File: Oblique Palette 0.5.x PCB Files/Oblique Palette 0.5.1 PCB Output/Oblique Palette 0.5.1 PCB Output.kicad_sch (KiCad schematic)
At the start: 16 parts, among them J40 Conn_01x03_Female_Pin, J42 AudioJack2_SwitchT, U11 MCP4725xxx-xCH, U12 MCP6004

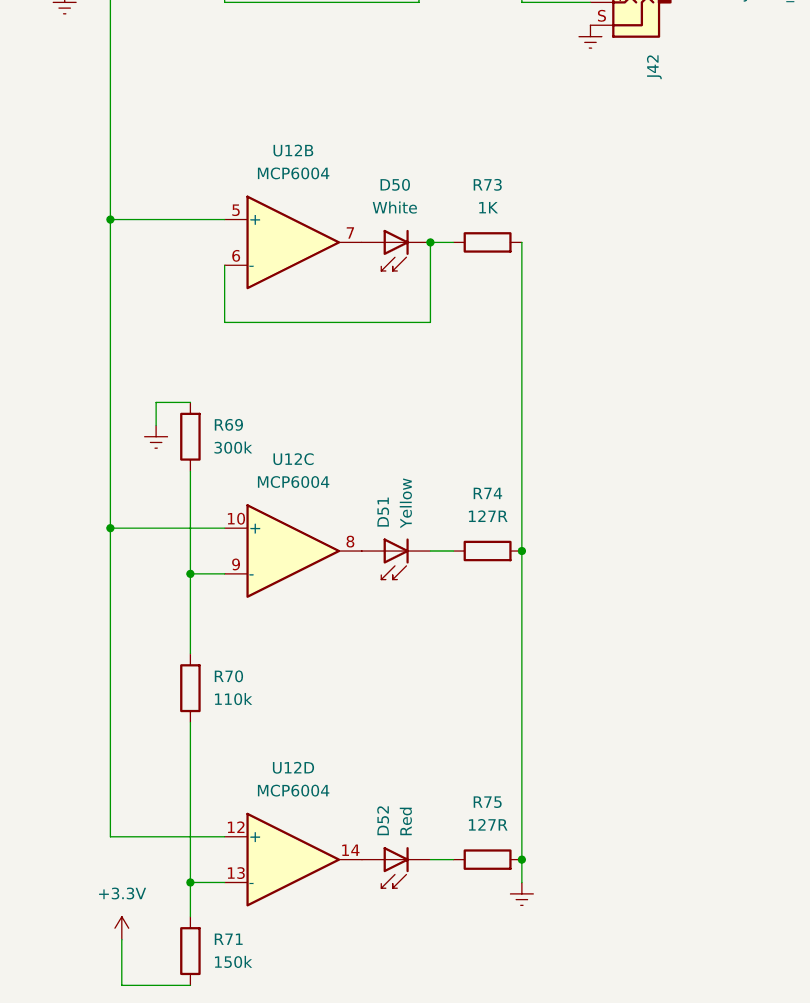
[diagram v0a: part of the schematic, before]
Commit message: Ready to go, but for some blank part numbers in the BOM to work out with the manufacturer.
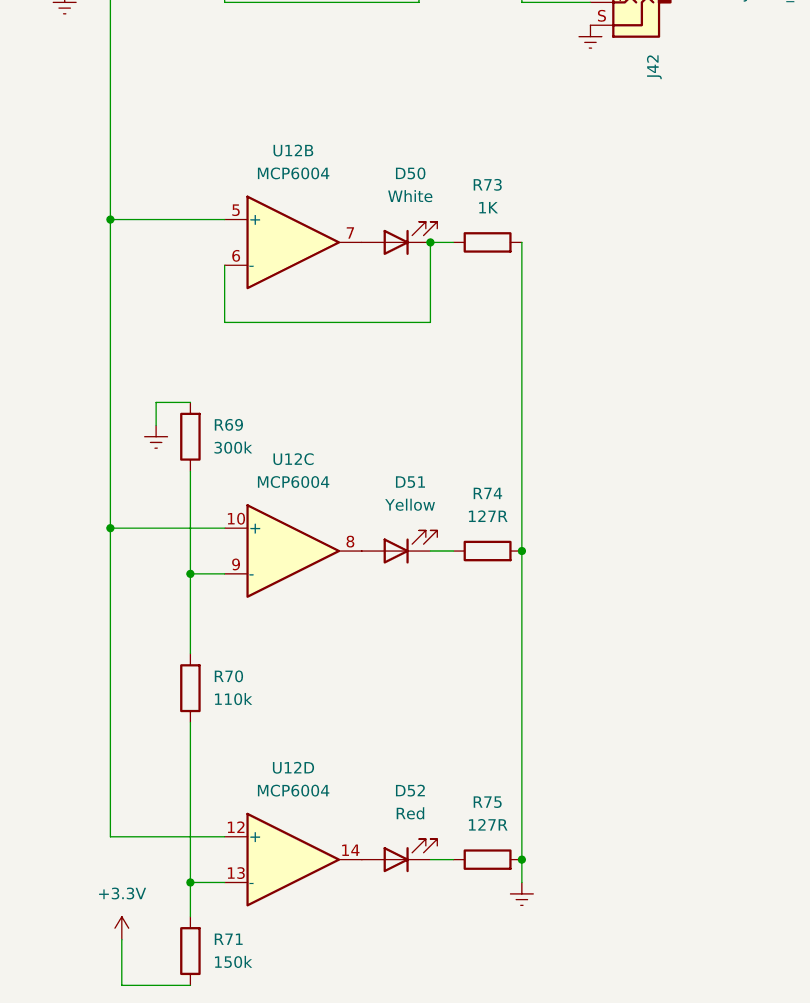
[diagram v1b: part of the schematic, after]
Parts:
- D50, D51, D52: footprint LED_THT:LED_SideEmitter_Rectangular_W4.5mm_H1.6mm -> LED_THT:LED_Rectangular_W5.0mm_H2.0mm; symbol LED:IRL81A -> Device:LED
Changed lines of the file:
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@@
 	)
 	(junction
-		(at 138.43 81.28)
+		(at 148.59 149.86)
 		(diameter 0)
 		(color 0 0 0 0)
 	)
 	(junction
-		(at 148.59 149.86)
+		(at 102.87 113.03)
 		(diameter 0)
 		(color 0 0 0 0)
 	)
 	(junction
-		(at 102.87 113.03)
+		(at 97.79 44.45)
 		(diameter 0)
 		(color 0 0 0 0)
 	)
 	(junction
-		(at 97.79 44.45)
+		(at 138.43 81.28)
 		(diameter 0)
 		(color 0 0 0 0)
@@
 	(wire
 		(pts
-			(xy 138.43 149.86) (xy 140.97 149.86)
+			(xy 138.43 81.28) (xy 140.97 81.28)
 		)
 		(stroke
@@
 	(wire
 		(pts
-			(xy 138.43 81.28) (xy 140.97 81.28)
+			(xy 102.87 113.03) (xy 115.57 113.03)
 		)
 		(stroke
@@
 	(wire
 		(pts
-			(xy 102.87 113.03) (xy 115.57 113.03)
+			(xy 107.95 99.06) (xy 107.95 101.6)
 		)
 		(stroke
@@
 	(wire
 		(pts
-			(xy 107.95 99.06) (xy 107.95 101.6)
+			(xy 62.23 46.99) (xy 63.5 46.99)
 		)
 		(stroke
@@
 	(wire
 		(pts
-			(xy 62.23 46.99) (xy 63.5 46.99)
+			(xy 73.66 52.07) (xy 73.66 54.61)
 		)
 		(stroke
@@
 	(wire
 		(pts
-			(xy 73.66 52.07) (xy 73.66 54.61)
+			(xy 111.76 134.62) (xy 111.76 152.4)
 		)
 		(stroke
@@
 	(wire
 		(pts
-			(xy 111.76 134.62) (xy 111.76 152.4)
+			(xy 148.59 81.28) (xy 148.59 115.57)
 		)
 		(stroke
@@
 	(wire
 		(pts
-			(xy 148.59 81.28) (xy 148.59 115.57)
+			(xy 138.43 149.86) (xy 140.97 149.86)
 		)
 		(stroke
@@
 	(wire
 		(pts
-			(xy 97.79 44.45) (xy 97.79 45.72)
+			(xy 138.43 115.57) (xy 140.97 115.57)
 		)
 		(stroke
@@
 	(wire
 		(pts
-			(xy 83.82 44.45) (xy 88.9 44.45)
+			(xy 97.79 44.45) (xy 97.79 45.72)
 		)
 		(stroke
@@
 	(wire
 		(pts
-			(xy 111.76 152.4) (xy 111.76 156.21)
+			(xy 83.82 44.45) (xy 88.9 44.45)
 		)
 		(stroke
@@
 	(wire
 		(pts
-			(xy 148.59 39.37) (xy 148.59 46.99)
+			(xy 111.76 152.4) (xy 111.76 156.21)
 		)
 		(stroke
@@
 	(wire
 		(pts
-			(xy 111.76 163.83) (xy 104.14 163.83)
+			(xy 148.59 39.37) (xy 148.59 46.99)
 		)
 		(stroke
@@
 	(wire
 		(pts
-			(xy 111.76 106.68) (xy 111.76 118.11)
+			(xy 111.76 163.83) (xy 104.14 163.83)
 		)
 		(stroke
@@
 	(wire
 		(pts
-			(xy 138.43 115.57) (xy 140.97 115.57)
+			(xy 111.76 106.68) (xy 111.76 118.11)
 		)
 		(stroke
@@
 	)
 	(symbol
-		(lib_id "LED:IRL81A")
-		(at 133.35 81.28 180)
+		(lib_id "Device:LED")
+		(at 134.62 81.28 180)
 		(unit 1)
 		(exclude_from_sim no)
@@
 		(fields_autoplaced yes)
 		(property "Reference" "D50"
-			(at 134.493 74.93 0)
+			(at 136.2075 73.66 0)
 			(effects
 				(font
@@
 		)
 		(property "Value" "White"
-			(at 134.493 77.47 0)
+			(at 136.2075 76.2 0)
 			(effects
 				(font
@@
 			)
 		)
-		(property "Footprint" "LED_THT:LED_SideEmitter_Rectangular_W4.5mm_H1.6mm"
-			(at 133.35 85.725 0)
+		(property "Footprint" "LED_THT:LED_Rectangular_W5.0mm_H2.0mm"
+			(at 134.62 81.28 0)
 			(effects
 				(font
@@
 			)
 		)
-		(property "Datasheet" "http://www.osram-os.com/Graphics/XPic0/00203825_0.pdf"
+		(property "Datasheet" "~"
 			(at 134.62 81.28 0)
 			(effects
@@
 			)
 		)
-		(property "Description" "850nm High Power Infrared Emitter, Side-Emitter package"
-			(at 133.35 81.28 0)
+		(property "Description" "WHITE Rectangular LED, diffused"
+			(at 134.62 81.28 0)
+			(effects
+				(font
+					(size 1.27 1.27)
+				)
+				(hide yes)
+			)
+		)
+		(property "Sim.Pins" "1=K 2=A"
+			(at 134.62 81.28 0)
 			(effects
 				(font
@@
 	)
 	(symbol
-		(lib_id "LED:IRL81A")
-		(at 133.35 115.57 180)
+		(lib_id "Device:LED")
+		(at 134.62 115.57 180)
 		(unit 1)
 		(exclude_from_sim no)
@@
 		(fields_autoplaced yes)
 		(property "Reference" "D51"
-			(at 133.2229 113.03 90)
+			(at 136.2075 107.95 0)
 			(effects
 				(font
 					(size 1.27 1.27)
 				)
-				(justify right)
 			)
 		)
 		(property "Value" "Yellow"
-			(at 135.7629 113.03 90)
+			(at 136.2075 110.49 0)
 			(effects
 				(font
 					(size 1.27 1.27)
 				)
-				(justify right)
 			)
 		)
-		(property "Footprint" "LED_THT:LED_SideEmitter_Rectangular_W4.5mm_H1.6mm"
-			(at 133.35 120.015 0)
+		(property "Footprint" "LED_THT:LED_Rectangular_W5.0mm_H2.0mm"
+			(at 134.62 115.57 0)
 			(effects
 				(font
@@
 			)
 		)
-		(property "Datasheet" "http://www.osram-os.com/Graphics/XPic0/00203825_0.pdf"
+		(property "Datasheet" "~"
 			(at 134.62 115.57 0)
 			(effects
@@
 			)
 		)
-		(property "Description" "850nm High Power Infrared Emitter, Side-Emitter package"
-			(at 133.35 115.57 0)
+		(property "Description" "YELLOW Rectangular LED, diffused"
+			(at 134.62 115.57 0)
+			(effects
+				(font
+					(size 1.27 1.27)
+				)
+				(hide yes)
+			)
+		)
+		(property "Sim.Pins" "1=K 2=A"
+			(at 134.62 115.57 0)
 			(effects
 				(font
@@
 	)
 	(symbol
-		(lib_id "LED:IRL81A")
-		(at 133.35 149.86 180)
+		(lib_id "Device:LED")
+		(at 134.62 149.86 180)
 		(unit 1)
 		(exclude_from_sim no)
@@
 		(fields_autoplaced yes)
 		(property "Reference" "D52"
-			(at 133.2229 147.32 90)
+			(at 136.2075 142.24 0)
 			(effects
 				(font
 					(size 1.27 1.27)
 				)
-				(justify right)
 			)
 		)
 		(property "Value" "Red"
-			(at 135.7629 147.32 90)
+			(at 136.2075 144.78 0)
 			(effects
 				(font
 					(size 1.27 1.27)
 				)
-				(justify right)
 			)
 		)
-		(property "Footprint" "LED_THT:LED_SideEmitter_Rectangular_W4.5mm_H1.6mm"
-			(at 133.35 154.305 0)
+		(property "Footprint" "LED_THT:LED_Rectangular_W5.0mm_H2.0mm"
+			(at 134.62 149.86 0)
+			(effects
+				(font
+					(size 1.27 1.27)
+				)
+				(hide yes)
+			)
+		)
+		(property "Datasheet" "~"
+			(at 134.62 149.86 0)
 			(effects
 				(font
@@
 			)
 		)
-		(property "Datasheet" "http://www.osram-os.com/Graphics/XPic0/00203825_0.pdf"
+		(property "Description" "RED Rectangular LED, diffused"
 			(at 134.62 149.86 0)
 			(effects
@@
 			)
 		)
-		(property "Description" "850nm High Power Infrared Emitter, Side-Emitter package"
-			(at 133.35 149.86 0)
+		(property "Sim.Pins" "1=K 2=A"
+			(at 134.62 149.86 0)
 			(effects
 				(font
